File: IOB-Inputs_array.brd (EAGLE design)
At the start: 104.1 x 106.7 mm, 83 parts, among them J1X11 RJ12/6, J1X12 RJ12/6, J1X13 RJ12/6, J1X14 RJ12/6

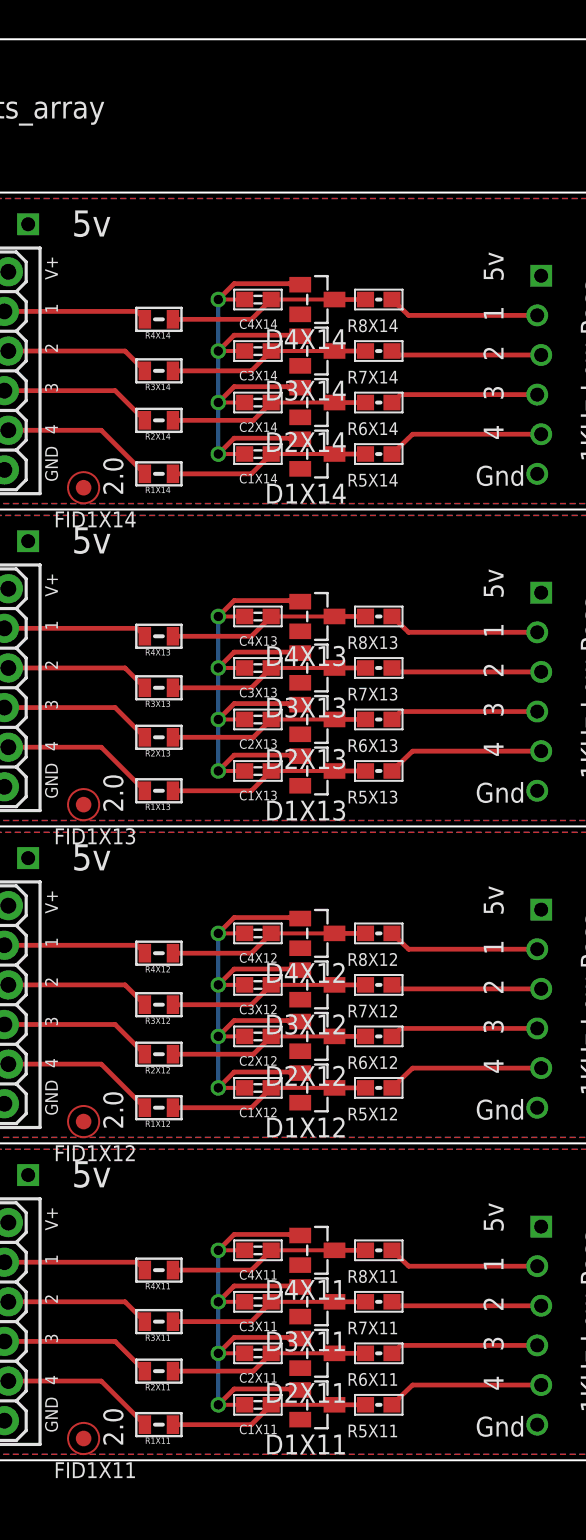
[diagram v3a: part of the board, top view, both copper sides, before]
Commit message: Rev to 2.1 because of Stencil change
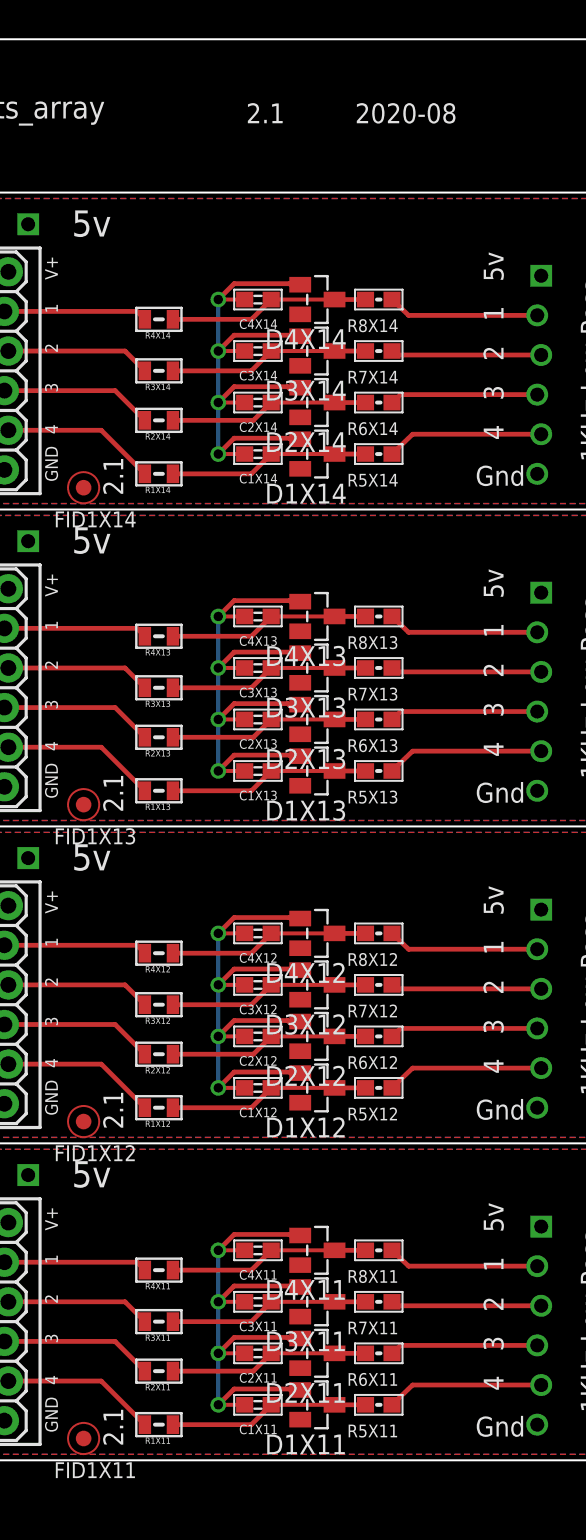
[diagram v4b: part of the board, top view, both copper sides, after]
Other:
- board text added: "2.1"
- board text removed: "2.0"
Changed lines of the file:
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@@
 <plain>
 <text x="27.686" y="14.351" size="1.27" layer="21" rot="R90">IO4-IOB</text>
-<text x="43.815" y="9.779" size="1.27" layer="21" rot="R90">2.0</text>
+<text x="43.815" y="9.779" size="1.27" layer="21" rot="R90">2.1</text>
 <text x="76.327" y="15.367" size="1.27" layer="21" rot="R90">Inputs</text>
 <text x="39.243" y="25.654" size="1.27" layer="22" rot="MR270">John Plocher</text>
@@
 <text x="81.28" y="12.7" size="1.27" layer="48" font="vector" ratio="10" rot="R90">Red Headers</text>
 <text x="27.686" y="34.671" size="1.27" layer="21" rot="R90">IO4-IOB</text>
-<text x="43.815" y="30.099" size="1.27" layer="21" rot="R90">2.0</text>
+<text x="43.815" y="30.099" size="1.27" layer="21" rot="R90">2.1</text>
 <text x="76.327" y="35.687" size="1.27" layer="21" rot="R90">Inputs</text>
 <text x="39.243" y="45.974" size="1.27" layer="22" rot="MR270">John Plocher</text>
@@
 <text x="81.28" y="33.02" size="1.27" layer="48" font="vector" ratio="10" rot="R90">Red Headers</text>
 <text x="27.686" y="54.991" size="1.27" layer="21" rot="R90">IO4-IOB</text>
-<text x="43.815" y="50.419" size="1.27" layer="21" rot="R90">2.0</text>
+<text x="43.815" y="50.419" size="1.27" layer="21" rot="R90">2.1</text>
 <text x="76.327" y="56.007" size="1.27" layer="21" rot="R90">Inputs</text>
 <text x="39.243" y="66.294" size="1.27" layer="22" rot="MR270">John Plocher</text>
@@
 <text x="81.28" y="53.34" size="1.27" layer="48" font="vector" ratio="10" rot="R90">Red Headers</text>
 <text x="27.686" y="75.311" size="1.27" layer="21" rot="R90">IO4-IOB</text>
-<text x="43.815" y="70.739" size="1.27" layer="21" rot="R90">2.0</text>
+<text x="43.815" y="70.739" size="1.27" layer="21" rot="R90">2.1</text>
 <text x="76.327" y="76.327" size="1.27" layer="21" rot="R90">Inputs</text>
 <text x="39.243" y="86.614" size="1.27" layer="22" rot="MR270">John Plocher</text>
@@
 <text x="47.244" y="73.8505" size="0.8128" layer="125" font="vector" rot="R180">R12</text>
 <text x="81.28" y="73.66" size="1.27" layer="48" font="vector" ratio="10" rot="R90">Red Headers</text>
+<text x="51.689" y="94.615" size="1.27" layer="21">2.1</text>
+<text x="58.674" y="94.615" size="1.27" layer="21">2020-08</text>
 </plain>
 <attributes>
